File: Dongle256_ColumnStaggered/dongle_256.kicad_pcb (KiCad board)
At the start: 2 copper layers, 138.1 x 98.1 mm, 61 parts, among them SW1 GateronLP, SW10 GateronLP, SW11 GateronLP, SW12 GateronLP, SW13 GateronLP, SW14 GateronLP, SW15 GateronLP, SW16 GateronLP, SW17 GateronLP, SW18 GateronLP, SW19 GateronLP, SW2 GateronLP, SW20 GateronLP, SW21 GateronLP, SW22 GateronLP, SW23 GateronLP, SW24 GateronLP, SW25 GateronLP, SW26 GateronLP, SW27 GateronLP, SW28 GateronLP, SW29 GateronLP, SW3 GateronLP, SW30 GateronLP, SW4 GateronLP, SW5 GateronLP, SW6 GateronLP, SW7 GateronLP, SW8 GateronLP, SW9 GateronLP, U1 NRF52840-DONGLE

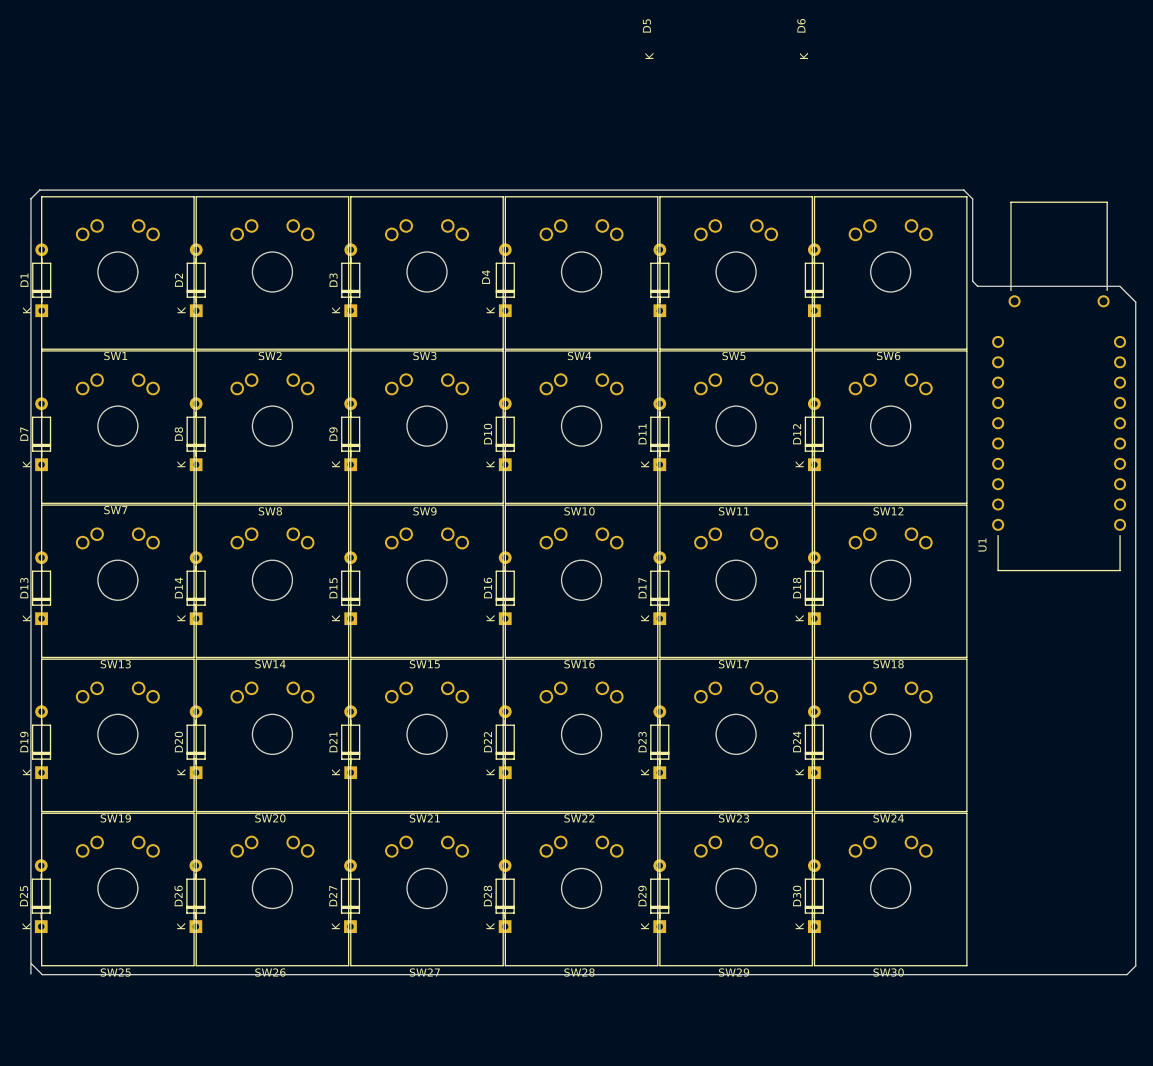
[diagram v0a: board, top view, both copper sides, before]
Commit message: PCB design without switch
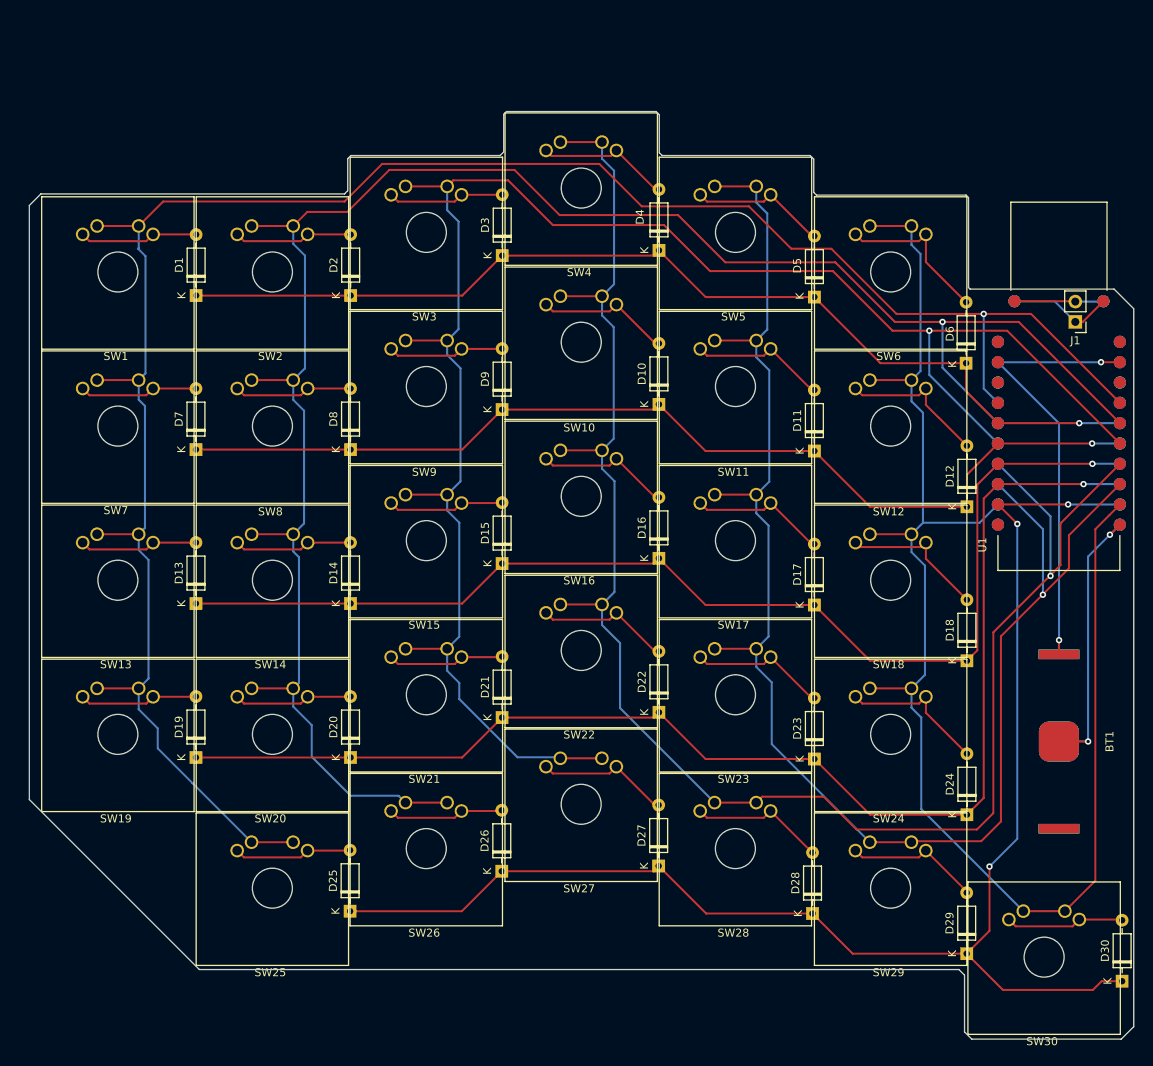
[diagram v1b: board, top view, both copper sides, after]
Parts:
- added BT1: Battery_Cell, MVB:TBH-CR2032-M04, F.Cu at (156.4, 109.8)
- added BT2 (x2): Battery_Cell, MVB:TBH-CR2032-M04, B.Cu at (156.4, 109.8)
- added J1: Conn_01x02_Male, Connector_PinHeader_2.54mm:PinHeader_1x02_P2.54mm_Vertical, F.Cu at (158.4, 57.4)
- added U2 (x2): NRF52840-DONGLE, download:MODULE_NRF52840-DONGLE, B.Cu at (156.4, 65.5)
- moved D27 39.3 mm to (106.4, 125.4)
- moved D30 39.1 mm to (164.3, 139.8)
- moved D26 38.9 mm to (86.8, 126.1)
- moved D25 38.7 mm to (67.8, 131.1)
- moved D29 38.5 mm to (144.9, 136.4)
- moved D28 38.5 mm to (125.6, 131.3)
- moved SW27 22.0 mm to (96.7, 117.7)
- moved SW30 21.0 mm to (154.6, 136.8)
- moved D10 20.6 mm to (106.4, 67.7)
- moved D16 20.6 mm to (106.4, 87.0)
- moved D22 20.6 mm to (106.4, 106.2)
- moved D4 20.6 mm to (106.4, 48.5)
- moved D15 20.1 mm to (86.8, 87.6)
- moved D21 20.1 mm to (86.8, 106.9)
- moved D3 20.1 mm to (86.8, 49.1)
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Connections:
- U1 pad 0.09: Net-(D10-Pad1) -> Net-(D19-Pad1)
- U1 pad 0.10: Net-(D1-Pad1) -> Net-(D25-Pad1)
- U1 pad 0.13: unconnected-(U1-Pad0.13) -> Net-(U1-Pad0.13)
- U1 pad 0.15: unconnected-(U1-Pad0.15) -> Net-(U1-Pad0.15)
- U1 pad 0.17: unconnected-(U1-Pad0.17) -> Net-(U1-Pad0.17)
- U1 pad 0.20: unconnected-(U1-Pad0.20) -> Net-(U1-Pad0.20)
- U1 pad 0.22: Net-(D25-Pad1) -> Net-(D1-Pad1)
- U1 pad 0.24: Net-(D19-Pad1) -> Net-(D10-Pad1)
- U1 pad OUT: unconnected-(U1-PadOUT) -> Net-(BT1-Pad1)
- U1 pad SWDCLK: unconnected-(U1-PadSWDCLK) -> Net-(J1-Pad1)
- U1 pad SWDIO: unconnected-(U1-PadSWDIO) -> Net-(J1-Pad2)
- U1 pad VBUS: unconnected-(U1-PadVBUS) -> Net-(U1-PadVBUS)
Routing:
- net Net-(SW1-Pad1): track 0.00 -> 261.4 mm, vias 0 -> 1
- net Net-(SW14-Pad1): track 0.00 -> 245.2 mm, vias 0 -> 1
- net Net-(SW15-Pad1): track 0.00 -> 225.9 mm, vias 0 -> 1
- net Net-(SW10-Pad1): track 0.00 -> 217.6 mm, vias 0 -> 1
- net Net-(SW11-Pad1): track 0.00 -> 194.4 mm, vias 0 -> 1
- net Net-(SW12-Pad1): track 0.00 -> 185.0 mm
- net Net-(D25-Pad1): track 0.00 -> 180.5 mm, vias 0 -> 3
- net Net-(D19-Pad1): track 0.00 -> 162.2 mm, vias 0 -> 1
- net Net-(D13-Pad1): track 0.00 -> 145.5 mm, vias 0 -> 1
- net Net-(D1-Pad1): track 0.00 -> 128.8 mm, vias 0 -> 1
- net Net-(D10-Pad1): track 0.00 -> 128.8 mm, vias 0 -> 1
- net Net-(BT1-Pad1): track 0.00 -> 56.7 mm, vias 0 -> 2
- net Net-(BT1-Pad2): track 0.00 -> 37.8 mm, vias 0 -> 2
- net Net-(D6-Pad2): track 0.00 -> 20.1 mm
- net Net-(D12-Pad2): track 0.00 -> 18.8 mm
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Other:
- board size 138.1 x 98.1 mm -> 138.1 x 116 mm

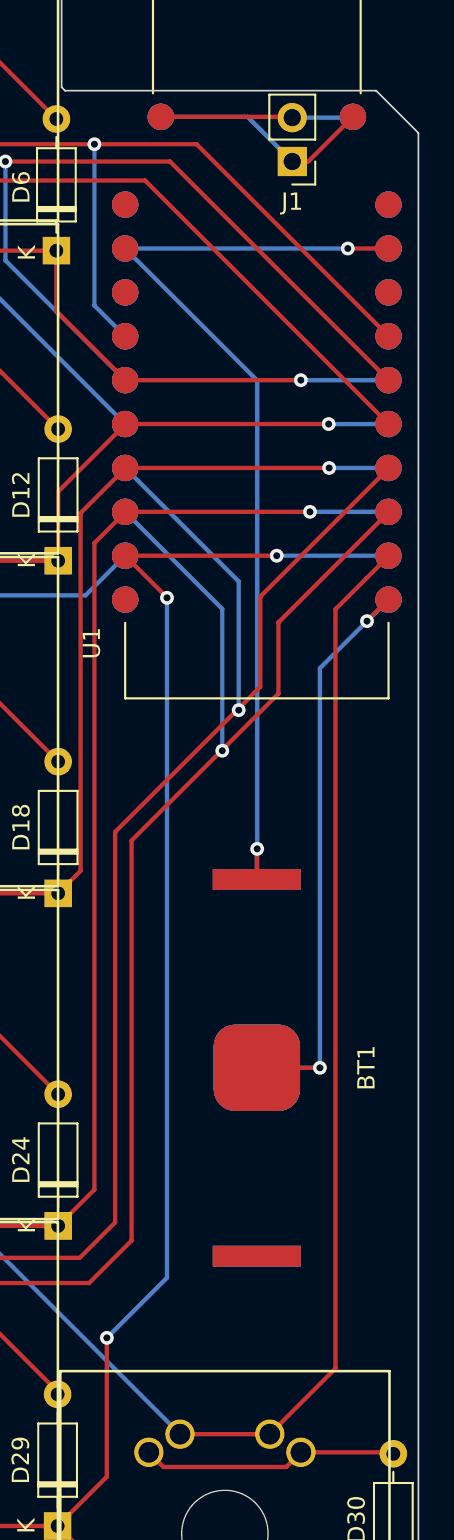
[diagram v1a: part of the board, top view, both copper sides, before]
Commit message: Update on off and slider switch
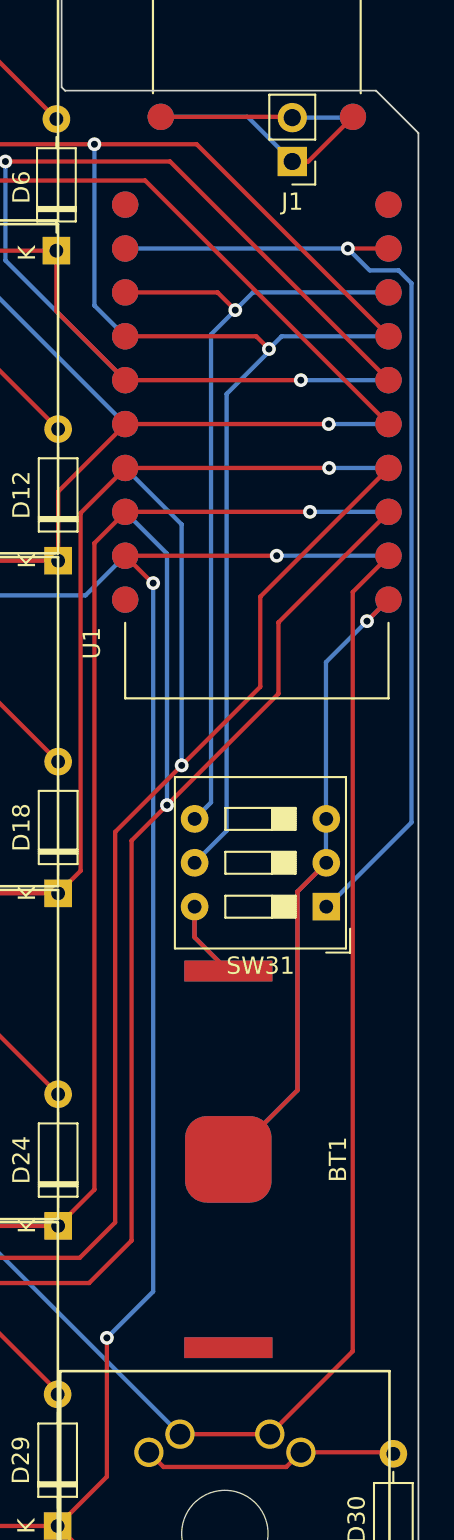
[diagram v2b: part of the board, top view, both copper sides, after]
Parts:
- removed the BT2 at (156.4, 109.8)
- removed the U2 at (156.4, 65.5)
- added SW31: SW_DIP_x03, Button_Switch_THT:SW_DIP_SPSTx03_Slide_9.78x9.8mm_W7.62mm_P2.54mm, F.Cu at (160.4, 100.5)
- moved BT1 5.55 mm to (154.8, 115.2)
- moved BT2 5.55 mm to (154.8, 115.2)
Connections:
- U1 pad OUT: Net-(BT1-Pad1) -> Net-(SW31-Pad1)
- U2 pad OUT: Net-(BT1-Pad1) -> Net-(SW31-Pad1)
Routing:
- net Net-(SW31-Pad1): track 0.00 -> 57.9 mm, vias 0 -> 1
- net Net-(BT1-Pad1): track 56.7 -> 9.07 mm, vias 2 -> 0
- net Net-(SW31-Pad5): track 0.00 -> 47.4 mm, vias 0 -> 1
- net Net-(SW31-Pad4): track 0.00 -> 46.5 mm, vias 0 -> 1
- net Net-(BT1-Pad2): track 37.8 -> 57.5 mm, vias 2 -> 1
- net Net-(SW11-Pad1): track 194.4 -> 196.2 mm
- net Net-(SW10-Pad1): track 217.6 -> 219.4 mm
- net Net-(D25-Pad1): track 180.5 -> 179.9 mm

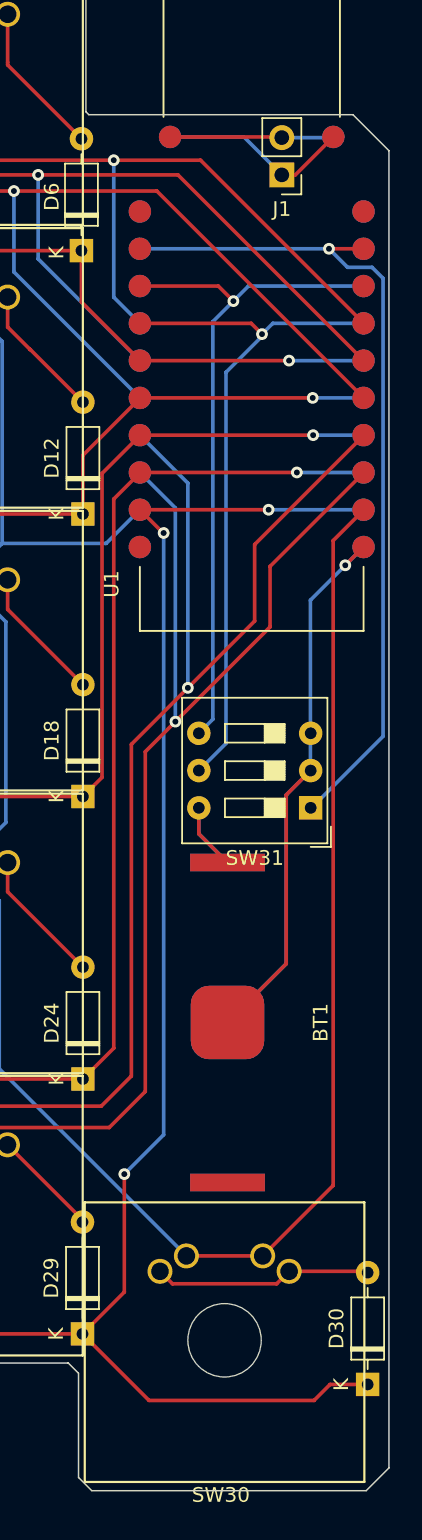
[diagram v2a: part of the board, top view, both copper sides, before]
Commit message: Update flashing pads and redo the status switch.
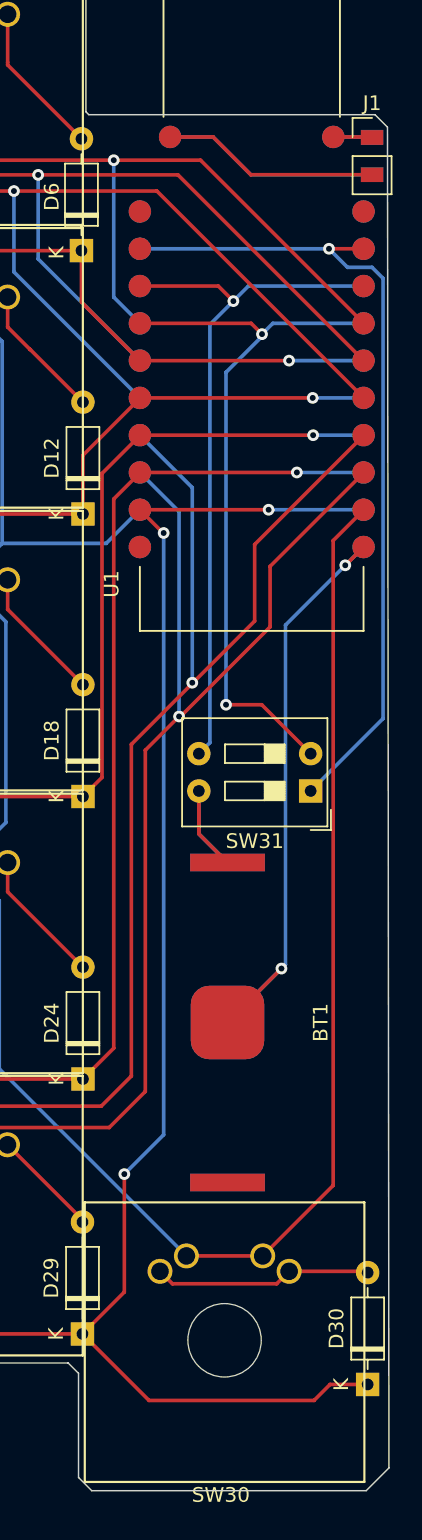
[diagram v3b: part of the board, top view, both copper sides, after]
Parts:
- added J2: Conn_01x02_Male, Connector_PinHeader_2.54mm:PinHeader_1x02_P2.54mm_Vertical, B.Cu at (164.6, 57.4)
- SW31: footprint Button_Switch_THT:SW_DIP_SPSTx03_Slide_9.78x9.8mm_W7.62mm_P2.54mm -> Button_Switch_THT:SW_DIP_SPSTx02_Slide_9.78x7.26mm_W7.62mm_P2.54mm
- moved J1 6.66 mm to (164.6, 54.9), turned to 0 degrees
- moved SW31 1.15 mm to (160.4, 99.4)
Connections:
- SW31 pad 2: Net-(BT1-Pad2) -> Net-(SW31-Pad2)
- SW31 pad 3: Net-(BT1-Pad2) -> Net-(U1-Pad0.17)
- SW31 pad 4: Net-(SW31-Pad4) -> Net-(BT1-Pad1)
- U1 pad 0.17: Net-(SW31-Pad4) -> Net-(U1-Pad0.17)
- U1 pad 0.20: Net-(SW31-Pad5) -> Net-(SW31-Pad2)
- U2 pad 0.17: Net-(SW31-Pad4) -> Net-(U1-Pad0.17)
- U2 pad 0.20: Net-(SW31-Pad5) -> Net-(SW31-Pad2)
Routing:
- net Net-(SW31-Pad2): track 0.00 -> 49.3 mm, vias 0 -> 2
- net Net-(U1-Pad0.17): track 0.00 -> 47.9 mm, vias 0 -> 1
- net Net-(SW31-Pad5): track 47.4 -> 0.00 mm, vias 1 -> 0
- net Net-(SW31-Pad4): track 46.5 -> 0.00 mm, vias 1 -> 0
- net Net-(BT1-Pad2): track 57.5 -> 43.2 mm, vias 1 -> 2
- net Net-(J1-Pad2): track 11.2 -> 17.5 mm
- net Net-(J1-Pad1): track 14.3 -> 17.7 mm
- net Net-(BT1-Pad1): track 9.07 -> 11.4 mm
- net Net-(U1-PadOUT): track 57.9 -> 56.7 mm
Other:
- outline, holes or cut-outs redrawn
